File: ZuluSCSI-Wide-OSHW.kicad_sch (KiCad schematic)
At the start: 182 parts, among them J1 USB_DATA, J2 TF003, J3 Conn_01x02, J4 MnL, J5 HD68, J6 Conn_01x05, J7 Conn_01x04, J8 Conn_01x02, Q1 AO3401A, Q10 AO3401A, Q11 AO3401A, Q12 AO3401A, Q13 AO3401A, Q14 AO3401A, Q15 AO3401A, Q16 AO3401A, Q17 AO3401A, Q18 AO3401A, Q19 AO3401A, Q2 AO3401A, Q20 AO3401A, Q21 AO3401A, Q22 AO3401A, Q23 AO3401A, Q24 AO3401A, Q25 AO3401A, Q26 AO3401A, Q27 AO3401A, Q3 AO3401A, Q4 AO3401A, Q5 AO3401A, Q6 AO3401A, Q7 AO3401A, Q8 AO3401A, Q9 AO3401A, SW1 SW_DIP_x04, SW2 GT-TC108A-H034-L1S, U1 RP2350_80QFN, U2 W25Q128JVS, U7 AZ1117-2.85, U8 AP62250WU, U9 USB TVS, Y1 12MHz

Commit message: Update schematic
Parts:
- gave numbers to parts that had none: 59
- renumbered C2 to C20, C3 to C21, C6 to C22, C8 to C23, C7 to C24, C10 to C25, C11 to C27, C12 to C28, C13 to C29, C14 to C30, C15 to C31, C16 to C32, C5 to C34, C16 to C38, C16 to C39, R5 to R14, R3 to R48, R4 to R49, R1 to R53, R3 to R65, U2 to U10
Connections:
- net BUS_DIR: now also U4.5; no longer U4.9
- net GND: now also U4.13, U4.4, U5.13, U5.4, U5.9; no longer U4.10, U4.10, U5.13, U5.2, U5.4
- net ~{BUS_DIR}: now also U4.1, U4.6, U5.1; no longer U4.10, U4.8, U5.10
- net ~{MCU_BSY_OUT}: now also U5.10; no longer U5.1
- net ~{MCU_SDP1}: now also U4.2; no longer U4.9
- net ~{MCU_SDP}: now also U5.2; no longer U5.9
- net ~{SCSI_BSY}: now also U5.12, U5.8; no longer U5.3, U5.5
- net ~{SCSI_SDP1}: now also U4.12, U4.3; no longer U4.8, U4.9
- net ~{SCSI_SDP}: now also U5.3, U5.5; no longer U5.12, U5.8
- net at R21.2: now also U5.11; no longer U5.6
- net at R19.1: now also U5.6; no longer U5.11
- net at R64.1: now also U4.11; no longer U4.8

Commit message: Make board ZuluSCSI firmware compatible
The initial design of the Wide OSHW had pin differences that were
incompatible with unmodified ZuluSCSI firmware with wide support.

The following changes were made:
 - The BUS_DIR changed polarity in the wide firmware thus the A and B
 side on the data buffers had to be swapped

 - 74LVT125 could no longer be used to for the parity pins on the
 data bus. Thus one was replaced with a 74LVT245. Only two of the eight
 bus pins are used on the new 74LVT245. Maybe a different part would
 make sense

 - All the data and control signal buffers have had their VCC changed
 from the 3.3V power to 2.85V power. A section of the 3.3V power
 plane was replace with a 2.85 power plane to support this change

 - The I2C pin along with the interrupt pin have changed position
 to take advantage of the hardware I2C support and mirror their location
 in the wide firmware

 - The UF2 bootloader switch has been removed from the DIP switch
 and replaced with a momentary contact switch

 - The eject button footprint has been laid down

 - The OSHW logo is now a top solder mask

 - Fonts used in the design have now been embedded
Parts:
- removed R19, R64: 1k, Resistor_SMD:R_0603_1608Metric, symbol Device:R
- removed R40: 4k7, Resistor_SMD:R_0603_1608Metric, symbol Device:R
- removed SW1: SW_DIP_x04, Button_Switch_SMD:SW_DIP_SPSTx04_Slide_6.7x11.72mm_W8.61mm_P2.54mm_LowProfile, symbol Switch:SW_DIP_x04
- removed U4: 74LVT125, Package_SO:TSSOP-14_4.4x5mm_P0.65mm, symbol 74xx:74LVC125
- added R18: 1k, Resistor_SMD:R_0603_1608Metric, symbol Device:R
- added SW1: SW_DIP_x03, Button_Switch_SMD:SW_DIP_SPSTx03_Slide_6.7x9.18mm_W8.61mm_P2.54mm_LowProfile, symbol Switch:SW_DIP_x03
- added SW3: SW_BOOT, ZuluSCSI-Wide-OSHW:SW-SMD_GT-TC108A-H034-L1S, symbol ZuluSCSI-Wide-OSHW:SW_Push_Mnt
- added U4: 74LVT245, Package_SO:SSOP-20_5.3x7.2mm_P0.65mm, symbol 74xx:74LS245
- H1: footprint GBSCSIZuluSCSI-Wide-OSHW:MH2.5_NPTH -> ZuluSCSI-Wide-OSHW:MH2.5_NPTH
- R43, R8: value 4k7 -> 2k; LCSC C23162 -> (none); LCSC Part # C23162 -> (none)
- SW2: value GT-TC108A-H034-L1S -> SW_EJECT; footprint (none) -> ZuluSCSI-Wide-OSHW:SW-SMD_GT-TC108A-H034-L1S; symbol Switch:SW_SPST -> ZuluSCSI-Wide-OSHW:SW_Push_Mnt; LCSC (none) -> C22396279; LCSC Part # (none) -> C22396279
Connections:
- net +2V8: now also C3.1, C37.1, C4.1, C5.1, C6.1, C7.1, R11.1, R12.1, R13.1, U11.20 (VCC), U2.20 (VCC), U3.20 (VCC), U5.1, U5.14 (VCC), U5.4, U6.14 (VCC), U4.20 (VCC)
- net +3V3: now also R18.1; no longer C3.1, C37.1, C4.1, C5.1, C6.1, C7.1, R11.1, R12.1, R13.1, U11.20 (VCC), U2.20 (VCC), U3.20 (VCC), U5.14 (VCC), U6.14 (VCC)
- net BUS_DIR: now also U11.1 (A->B), U2.1 (A->B), U4.1 (A->B)
- net EJECT: now also SW2.2; no longer SW2.1 (A)
- net GND: now also SW2.1, SW2.3 (MNT), U5.2, U5.5, SW1.1, SW1.2, SW1.3, SW3.1, SW3.3 (MNT), U4.10 (GND), U4.19 (CE); no longer SW2.2 (B), U5.4
- net I²C_INT: now also U1.37 (GPIO29); no longer U1.39 (GPIO31)
- net I²C_SCL: now also U1.39 (GPIO31); no longer U1.38 (GPIO30)
- net I²C_SDA: now also U1.38 (GPIO30); no longer U1.37 (GPIO29)
- net ~{INITIATOR}: now also SW1.6
- net ~{MCU_SD0}: now also U2.9 (A7); no longer U2.11 (B7)
- net ~{MCU_SD10}: now also U11.4 (A2); no longer U11.16 (B2)
- net ~{MCU_SD11}: now also U11.5 (A3); no longer U11.15 (B3)
- net ~{MCU_SD12}: now also U11.6 (A4); no longer U11.14 (B4)
- net ~{MCU_SD13}: now also U11.7 (A5); no longer U11.13 (B5)
- net ~{MCU_SD14}: now also U11.8 (A6); no longer U11.12 (B6)
- net ~{MCU_SD15}: now also U11.9 (A7); no longer U11.11 (B7)
- net ~{MCU_SD1}: now also U2.8 (A6); no longer U2.12 (B6)
- net ~{MCU_SD2}: now also U2.7 (A5); no longer U2.13 (B5)
- net ~{MCU_SD3}: now also U2.6 (A4); no longer U2.14 (B4)
- net ~{MCU_SD4}: now also U2.5 (A3); no longer U2.15 (B3)
- net ~{MCU_SD5}: now also U2.4 (A2); no longer U2.16 (B2)
- net ~{MCU_SD6}: now also U2.3 (A1); no longer U2.17 (B1)
- net ~{MCU_SD7}: now also U2.2 (A0); no longer U2.18 (B0)
- net ~{MCU_SD8}: now also U11.2 (A0); no longer U11.18 (B0)
- net ~{MCU_SD9}: now also U11.3 (A1); no longer U11.17 (B1)
- net ~{MCU_SDP1}: now also U4.3 (A1)
- net ~{MCU_SDP}: now also U4.2 (A0); no longer U5.2
- net ~{SCSI_SD0}: now also U2.11 (B7); no longer U2.9 (A7)
- net ~{SCSI_SD10}: now also U11.16 (B2); no longer U11.4 (A2)
- net ~{SCSI_SD11}: now also U11.15 (B3); no longer U11.5 (A3)
- net ~{SCSI_SD12}: now also U11.14 (B4); no longer U11.6 (A4)
- net ~{SCSI_SD13}: now also U11.13 (B5); no longer U11.7 (A5)
- net ~{SCSI_SD14}: now also U11.12 (B6); no longer U11.8 (A6)
- net ~{SCSI_SD15}: now also U11.11 (B7); no longer U11.9 (A7)
- net ~{SCSI_SD1}: now also U2.12 (B6); no longer U2.8 (A6)
- net ~{SCSI_SD2}: now also U2.13 (B5); no longer U2.7 (A5)
- net ~{SCSI_SD3}: now also U2.14 (B4); no longer U2.6 (A4)
- net ~{SCSI_SD4}: now also U2.15 (B3); no longer U2.5 (A3)
- net ~{SCSI_SD5}: now also U2.16 (B2); no longer U2.4 (A2)
- net ~{SCSI_SD6}: now also U2.17 (B1); no longer U2.3 (A1)
- net ~{SCSI_SD7}: now also U2.18 (B0); no longer U2.2 (A0)
- net ~{SCSI_SD8}: now also U11.18 (B0); no longer U11.2 (A0)
- net ~{SCSI_SD9}: now also U11.17 (B1); no longer U11.3 (A1)
- net ~{SCSI_SDP1}: now also U4.17 (B1)
- net ~{SCSI_SDP}: now also U4.18 (B0); no longer U5.3, U5.5
- net ~{TERM_EN}: now also R18.2, SW1.4
- net ~{USB_BOOT}: now also SW3.2
- net at R6.2, R9.1: now also SW1.5
- removed net ~{BUS_DIR}: U11.1 (A->B), U2.1 (A->B), U5.1
- no-connect marks 14 -> 28
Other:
- note added: "I²C_INT with a 68 Pin conn must be pulled up With a SCA conn must be pulled down and will no longer work as an Interrupt pin"
- moved on the sheet: J8, U5A, U5B

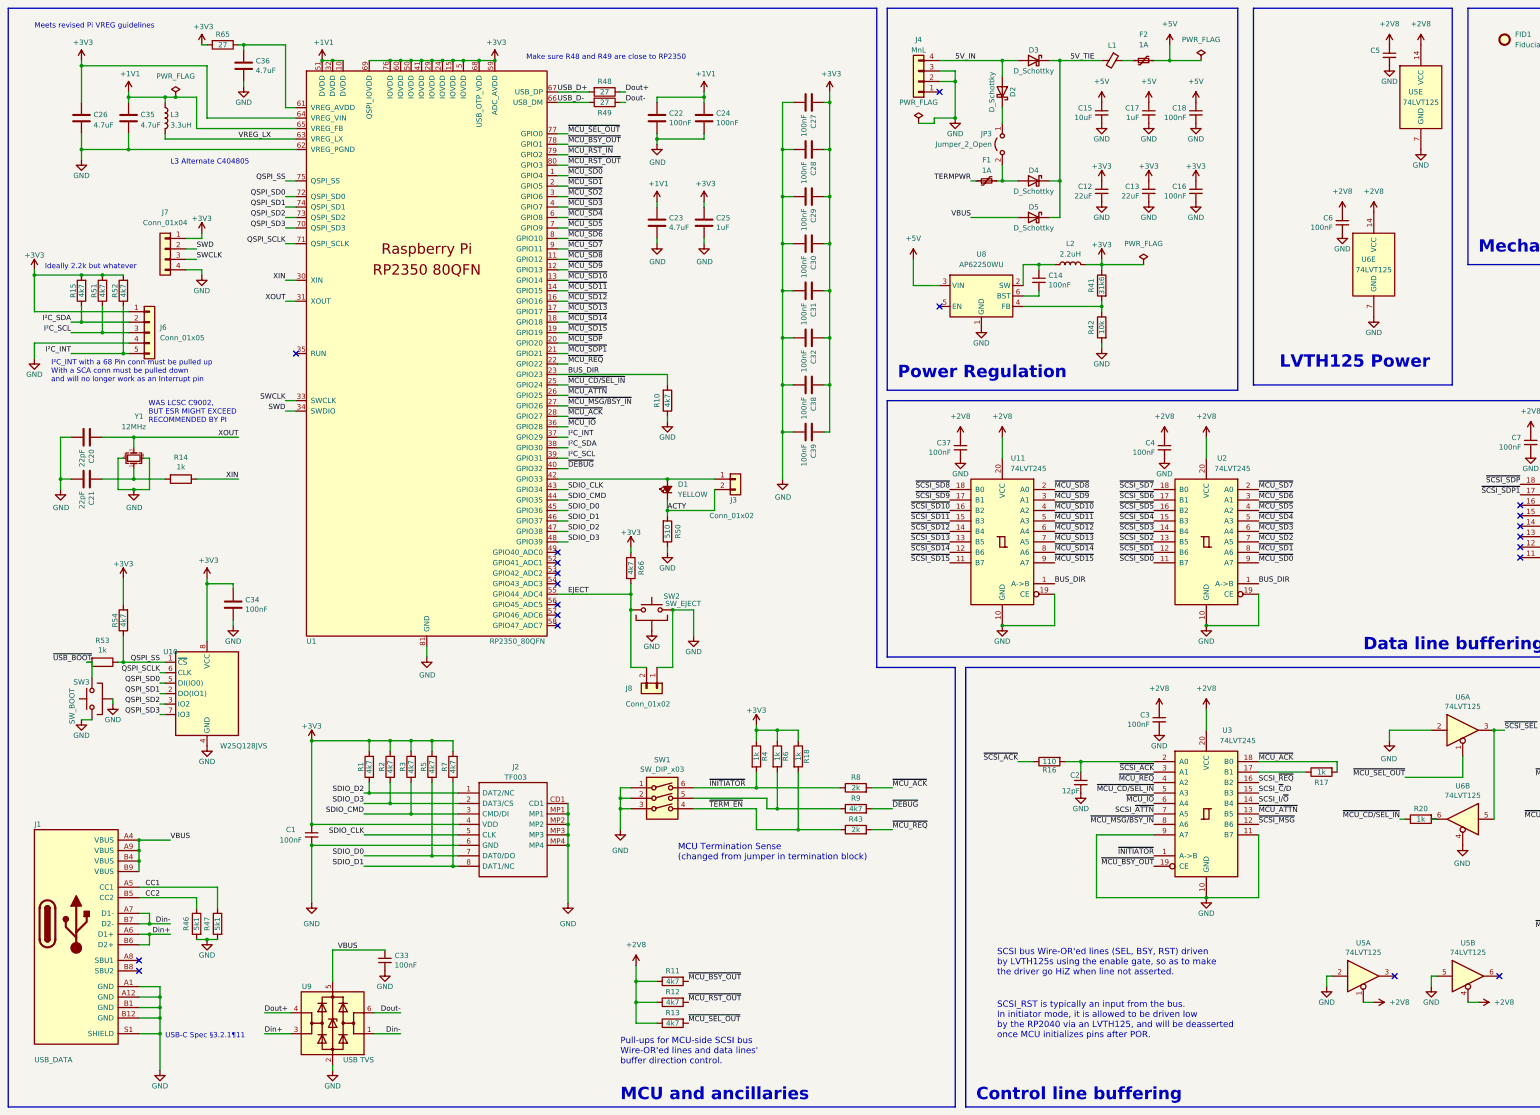
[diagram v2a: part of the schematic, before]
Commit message: PCB Update, Layout and DRC passed for rev 2026a
Schematic updated with more features from the ZuluSCSI wide board.
JLCPCB parts orientation and position adjusted.
Silkscreen updated

Features added:
- Pico SWD debug header (3 Pin JST header)
- I2C QWIIC header added (4 pin JST header)
- I2S Header added, compatible with AdaFruit PCM510x I2S DACs
- 4 Pin 0.1" (2.54mm) pitch power header added
- Github Workflow for auto generation of Gerbers, BOM, and Pos files
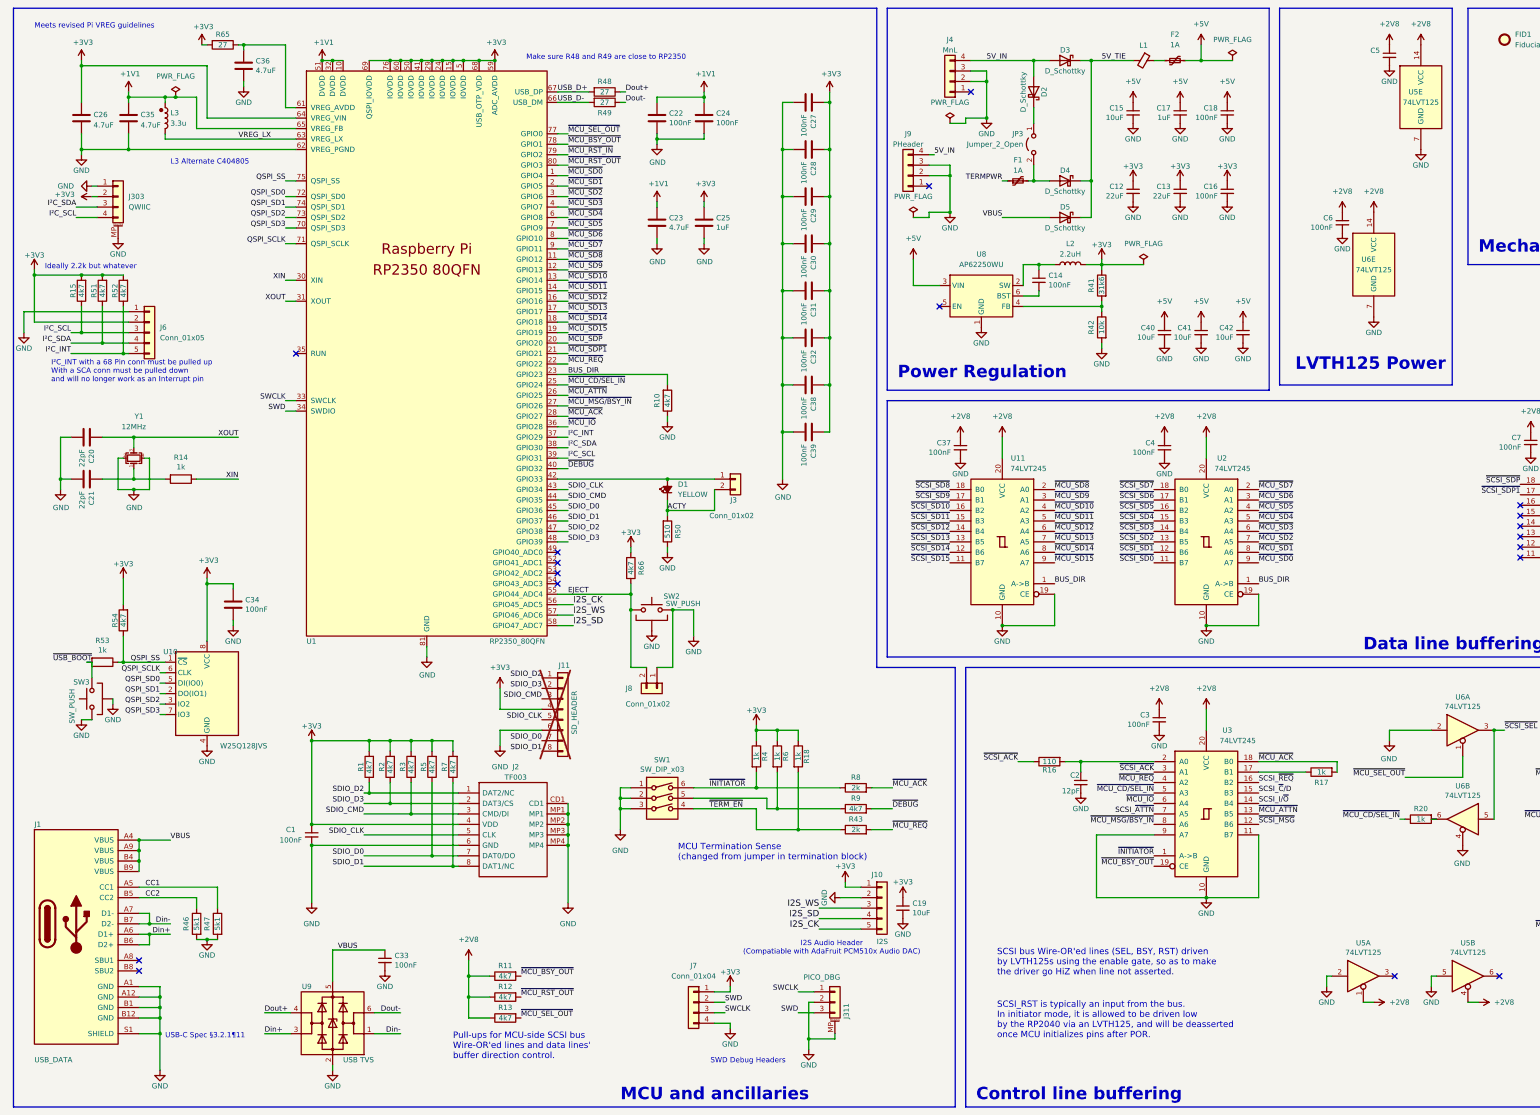
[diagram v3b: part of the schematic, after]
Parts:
- removed L3: 3.3uH, Inductor_SMD:L_1008_2520Metric_Pad1.43x2.20mm_HandSolder, symbol Device:L
- added C19, C40, C41, C42: 10uF, Capacitor_SMD:C_0603_1608Metric, symbol Device:C_Small
- added J10: I2S, ZuluSCSI-Wide-OSHW:PCM510x_1x05_P2.54mm_Vertical, symbol Connector_Generic:Conn_01x05
- added J11: SD_HEADER, Connector_PinHeader_2.54mm:PinHeader_1x08_P2.54mm_Vertical, symbol Connector_Generic:Conn_01x08
- added J303: QWIIC, Connector_JST:JST_SH_BM04B-SRSS-TB_1x04-1MP_P1.00mm_Vertical, symbol Connector_Generic_MountingPin:Conn_01x04_MountingPin
- added J311: PICO_DBG, Connector_JST:JST_SH_BM03B-SRSS-TB_1x03-1MP_P1.00mm_Vertical, symbol Connector_Generic_MountingPin:Conn_01x03_MountingPin
- added J9: PHeader, Connector_PinHeader_2.54mm:PinHeader_1x04_P2.54mm_Vertical, symbol Connector_Generic:Conn_01x04
- added L3: 3.3u, ZuluSCSI-Wide-OSHW:L_pol_2016, symbol zuluscsi:Abacron_AOTA-B201610S3R3-101-T
- F1, F2: LCSC C468888 -> C70061; LCSC Part # C468888 -> C70061
- FID1, J3, J4, J7, J8: now left out of the parts list
- J1: JLCPCBCORRECT (none) -> 0;-1.395;0
- J2: JLCPCBCORRECT (none) -> 0;-2.115;0
- J5, J6: LCSC (none) -> N/A; LCSC Part # (none) -> N/A; now left out of the parts list
- L2: footprint Inductor_SMD:L_Vishay_IHLP-2525 -> Inductor_SMD:L_1008_2520Metric_Pad1.43x2.20mm_HandSolder; LCSC C540967 -> C86092; LCSC Alt (none) -> C315721; LCSC Part # C540967 -> C86092; Manufacturer (none) -> Murata Electronics North America; PartNumber (none) -> DFE252012P-2R2M=P2; digikey (none) -> 490-10649-1-ND; mouser (none) -> 81-DFE252012P-2R2MP2
- Q1, Q10, Q11, Q12, Q13, Q14, Q15, Q16, Q17, Q18, Q19, Q2, Q20, Q21, Q22, Q23, Q24, Q25, Q26, Q27, Q3, Q4, Q5, Q6, Q7, Q8, Q9, U7, U8: JLCPCBCORRECT (none) -> 0;0;180
- R43, R8: LCSC (none) -> C22975; LCSC Part # (none) -> C22975
- SW2: value SW_EJECT -> SW_PUSH
- SW3: value SW_BOOT -> SW_PUSH
- U1: LCSC C9900136995 -> C42415655; LCSC Part # C9900136995 -> C42415655
- U10, U5, U6, U9: JLCPCBCORRECT (none) -> 0;0;-90
- U11, U2, U3, U4: JLCPCBCORRECT (none) -> 0;0;-90; LCSC C2652121 -> C74214; LCSC Part # C2652121 -> C74214
- Y1: LCSC C133334 -> C20625731; LCSC Part # C133334 -> C20625731; Manufacturer (none) -> Abracon LLC; PartNumber (none) -> ABM8-272-T3; digikey (none) -> 535-ABM8-272-T3TR-ND; mouser (none) -> 815-ABM8-272-T3
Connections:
- net +1V1: now also L3.1
- net +3V3: now also J6.2 (Pin_2), C19.1, J10.1 (Pin_1), J11.4 (Pin_4), J303.2 (Pin_2); no longer J6.1 (Pin_1)
- net +5V: now also C40.1, C41.1, C42.1
- net 5V_IN: now also J9.4 (Pin_4)
- net GND: now also J6.1 (Pin_1), C19.2, C40.2, C41.2, C42.2, J10.2 (Pin_2), J11.6 (Pin_6), J303.1 (Pin_1), J303.MP (MountPin), J311.2 (Pin_2), J311.MP (MountPin), J9.2 (Pin_2), J9.3 (Pin_3); no longer J6.4 (Pin_4)
- net I²C_SCL: now also R15.1, J303.4 (Pin_4); no longer R51.1
- net I²C_SDA: now also J6.4 (Pin_4), R51.1, J303.3 (Pin_3); no longer J6.2 (Pin_2), R15.1
- net SDIO_CLK: now also J11.5 (Pin_5)
- net SDIO_CMD: now also J11.3 (Pin_3)
- net SDIO_D0: now also J11.7 (Pin_7)
- net SDIO_D1: now also J11.8 (Pin_8)
- net SDIO_D2: now also J11.1 (Pin_1)
- net SDIO_D3: now also J11.2 (Pin_2)
- net SWCLK: now also J311.1 (Pin_1)
- net SWD: now also J311.3 (Pin_3)
- net VREG_LX: now also L3.2
- net I2S_CK: now reaches U1.56 (GPIO45_ADC5)
- net I2S_CK: now also J10.5 (Pin_5)
- net I2S_WS: now reaches U1.57 (GPIO46_ADC6)
- net I2S_WS: now also J10.3 (Pin_3)
- net I2S_SD: now reaches U1.58 (GPIO47_ADC7)
- net I2S_SD: now also J10.4 (Pin_4)
- no-connect marks 28 -> 26
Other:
- note added: "I2S Audio Header (Compatiable with AdaFruit PCM510x Audio DAC)"
- note added: "SWD Debug Headers"
- note removed: "WAS LCSC C9002, BUT ESR MIGHT EXCEED RECOMMENDED BY PI"
- title: ZuluSCSI Wide OSHW -> ZuluSCSI Ultra Wide OSHW
- moved on the sheet: C12, C13, C15, C16, C17, C18, D2, D3, D4, D5, F1, F2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
